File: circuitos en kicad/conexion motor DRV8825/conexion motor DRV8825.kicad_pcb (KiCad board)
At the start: 2 copper layers, 60.2 x 45 mm, 29 parts, among them P1 CONN_3X2, P10 CONN_2, P2 CONN_2, P3 CONN_2, P4 CONN_2, P5 CONN_2, P6 CONN_2, P7 CONN_2, P8 CONN_2, P9 CONN_2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

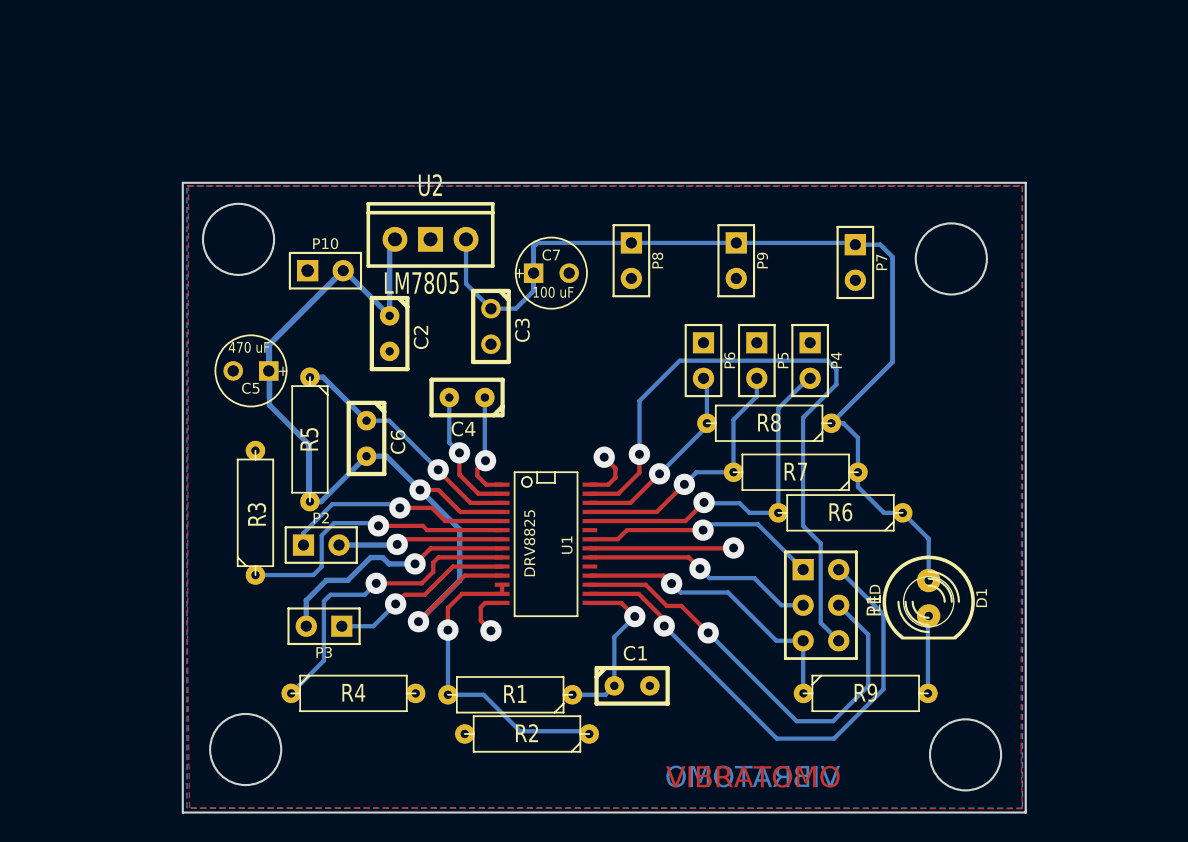
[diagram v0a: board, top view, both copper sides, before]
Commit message: Placa del DRV8825 actualizada al 25/07/2014
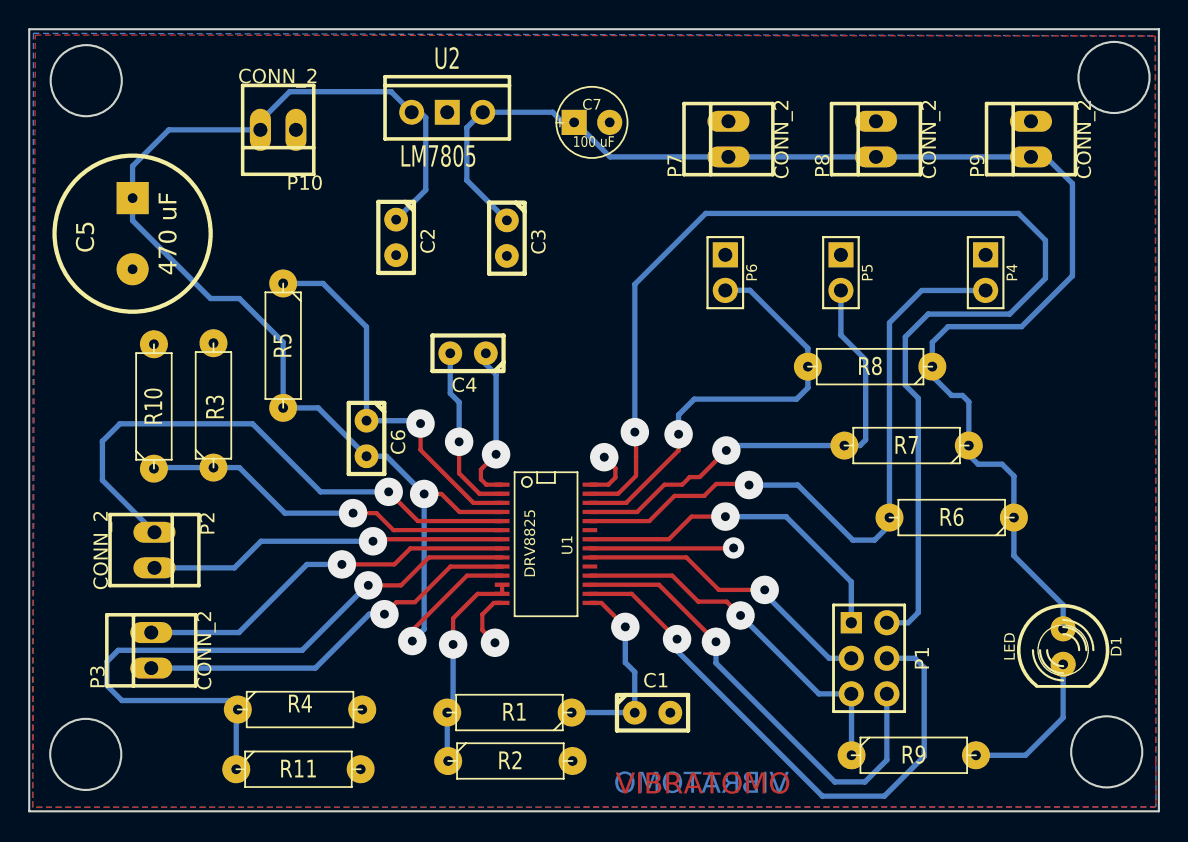
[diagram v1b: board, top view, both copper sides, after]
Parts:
- added R10: R, R3-5, F.Cu at (175.9, 93.6)
- added R11: R, R3-5, F.Cu at (186.3, 119.5)
- C5: footprint C1V5 -> C2V10
- P10, P2, P3, P7, P8, P9: footprint PIN_ARRAY_2X1 -> PINHEAD1-2
- moved P9 22.8 mm to (238.6, 74.5), turned to 90 degrees
- moved P8 19.5 mm to (227.5, 74.5), turned to 90 degrees
- moved P4 14.0 mm to (235.4, 84.0)
- moved C5 12.9 mm to (174.4, 81.3), turned to 270 degrees
- moved P7 12.6 mm to (217.0, 74.5), turned to 90 degrees
- moved P3 12.5 mm to (175.8, 111.0), turned to 90 degrees
- moved P2 11.9 mm to (176.0, 103.9), turned to 270 degrees
- moved C7 11.2 mm to (207.2, 73.3)
- moved P10 10.6 mm to (184.8, 73.8), turned to 180 degrees
- moved D1 10.2 mm to (240.9, 110.8)
- moved U2 9.16 mm to (196.9, 72.6)
- moved P5 8.69 mm to (225.0, 84.0)
- moved R8 8.27 mm to (227.1, 90.8)
- moved R3 8.24 mm to (180.2, 93.5)
- moved R7 8.15 mm to (229.7, 96.4)
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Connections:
- net N-0000014 renamed STEP
- net N-000005 renamed FAUL
- P1 pad 2: N-0000017 (its old number) -> HOME
- P1 pad 3: N-0000016 (its old number) -> DIR
- P1 pad 4: N-0000020 (its old number) -> RESET
- P1 pad 6: N-0000018 (its old number) -> SLEEP
- U1 pad 16: N-0000017 (its old number) -> RESET
- U1 pad 17: N-0000020 (its old number) -> SLEEP
- U1 pad 20: N-0000016 (its old number) -> DIR
- U1 pad 27: N-0000018 (its old number) -> HOME
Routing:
- net HOME: track 0.00 -> 86.9 mm, vias 0 -> 1
- net N-0000018 (its old number): track 46.2 -> 0.00 mm, vias 1 -> 0
- net RESET: track 0.00 -> 40.8 mm, vias 0 -> 1
- net N-0000017 (its old number): track 36.9 -> 0.00 mm, vias 1 -> 0
- net SLEEP: track 0.00 -> 33.3 mm, vias 0 -> 1
- net N-0000020 (its old number): track 31.6 -> 0.00 mm, vias 1 -> 0
- net N-0000018: track 22.0 -> 47.4 mm
- net N-0000024: track 16.4 -> 40.0 mm
- net N-000004: track 24.9 -> 46.9 mm
- net DIR: track 0.00 -> 21.8 mm, vias 0 -> 1
- net N-000003: track 14.2 -> 30.9 mm
- net N-0000016 (its old number): track 16.6 -> 0.00 mm, vias 1 -> 0
- net N-0000017: track 13.2 -> 28.1 mm
- net N-000002: track 18.8 -> 33.2 mm
- net N-0000020: track 12.3 -> 25.7 mm
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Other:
- board size 60.2 x 45 mm -> 80.7 x 55.9 mm
- net class Default: trace_width 0.381 -> 0.3048; via_dia 1.524 -> 2.032
